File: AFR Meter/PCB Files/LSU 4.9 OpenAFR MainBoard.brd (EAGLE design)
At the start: 62 x 83.5 mm, 82 parts, among them IC2 LMV321M5X, IC3 MCP4725A2T-E_CH, IC4 ATMEGA328PB-AN, IC5 ISO6520DR, IC6 7805DT, IC7 MCP25625-E_SS, Q1 BUK7Y6R0-60EX

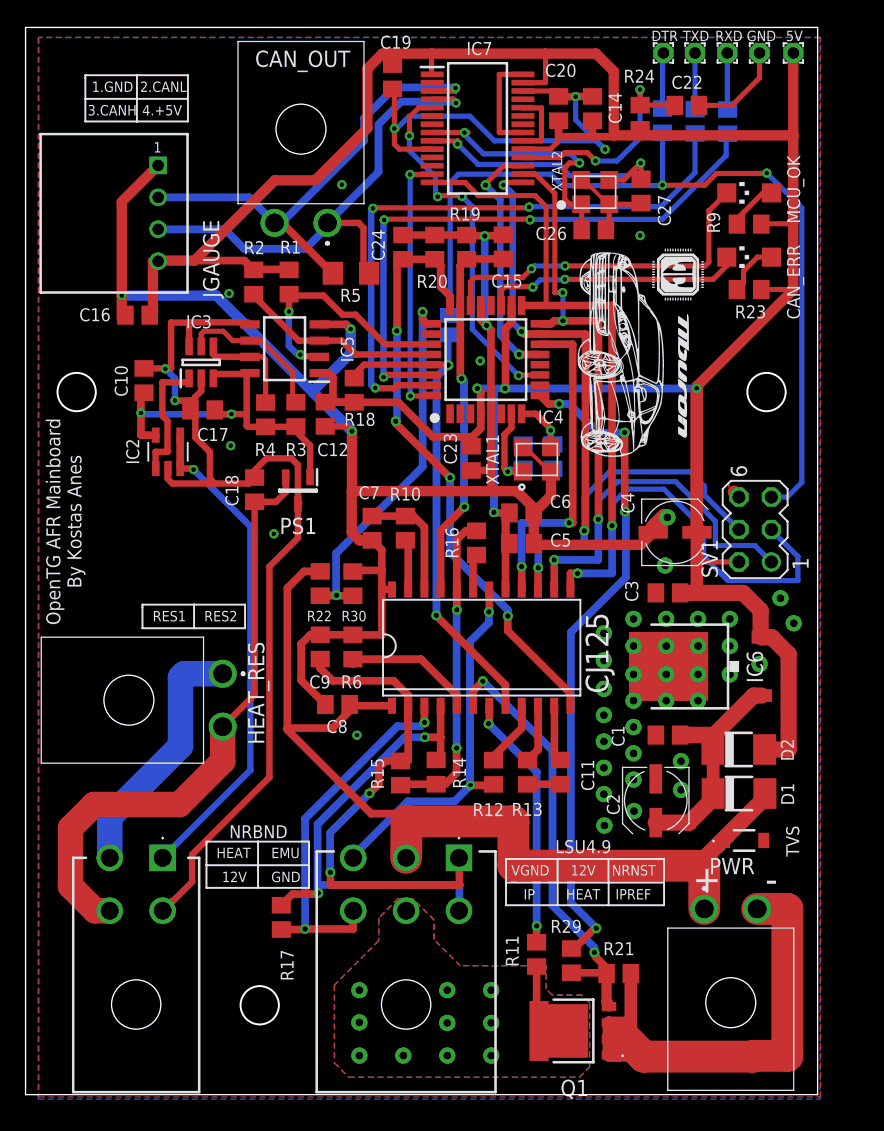
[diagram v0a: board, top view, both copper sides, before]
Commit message: QoL changes for optimizing production
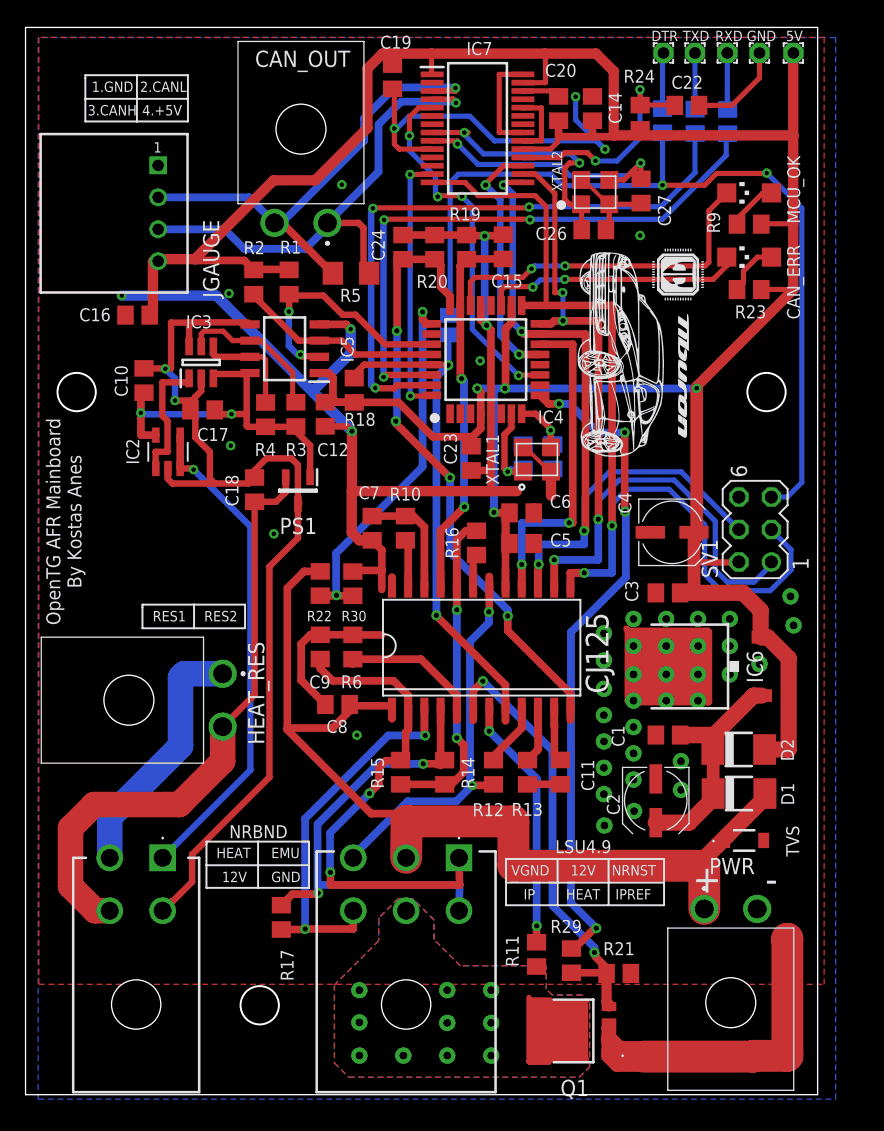
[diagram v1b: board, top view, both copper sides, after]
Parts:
- moved R14 0.67 mm to (32.8, 25.2)
- moved C4 0.23 mm to (50.6, 44.0)
- moved R15 0.06 mm to (29.4, 25.2)
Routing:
- net GND: track 256.8 -> 237.2 mm, vias 49 -> 47
- net LSU_HEAT: track 7.53 -> 17.0 mm
- net SPI_MISO: track 62.2 -> 65.0 mm
- net LSU_IPREF: track 40.7 -> 39.3 mm
- net RESET: track 108.4 -> 109.5 mm
- net LSU_VGND: track 29.4 -> 30.6 mm
- net HEAT_GATE: track 34.6 -> 35.7 mm
- net N$7: track 10.5 -> 11.7 mm
- net UR: track 47.9 -> 49.0 mm
- net +12V: track 80.5 -> 81.5 mm
- net USUP: track 24.9 -> 25.8 mm
- net LSU_IP: track 29.6 -> 30.3 mm

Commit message: Mainboard power supply and QoL updates.
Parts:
- removed C2, C4: 10uF, rcl:UD-5X5,8_NICHICON
- removed IC6: 7805DT, linear:TO252
- added C28: 10uF, rcl:C0805
- added C29, C30: (no value), rcl:153CLV-0605
- added IC1: MC7805CD2TR4G, MC7805CD2TR4G:MC7805CD2TR4G
- moved C3 2.40 mm to (50.9, 41.6)
- moved SV1 2.28 mm to (57.5, 46.5)
- moved C1 1.15 mm to (50.6, 27.0)
- moved C8 0.77 mm to (23.6, 30.5)
- moved C9 0.77 mm to (22.3, 35.0)
- moved R22 0.77 mm to (22.3, 40.0)
- moved R30 0.77 mm to (24.9, 40.0)
- moved R6 0.77 mm to (24.9, 35.0)
- moved U$1 0.72 mm to (35.1, 35.1)
- moved C5 0.67 mm to (39.4, 43.5)
- moved R10 0.58 mm to (29.3, 44.7)
- moved C6 0.55 mm to (39.4, 45.6)
- moved C7 0.43 mm to (26.9, 44.7)
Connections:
- new net N$4: C21.1, RESET.1
- net +5V: now also C29.+, IC1.3; no longer C4.+, IC6.2
- net 5V_ISO: now also C28.1
- net GND: now also C29.-, C30.-, IC1.2; no longer C2.-, C4.-, IC6.3
- net N$6: now also C30.+, IC1.1; no longer C2.+, IC6.1
- net NRBND_GND: now also C28.2
- net RESET: no longer C21.1, RESET.1, SV1.5
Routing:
- net GND: track 237.2 -> 132.8 mm, vias 47 -> 45
- net RESET: track 109.5 -> 41.3 mm, vias 4 -> 2
- net N$4: track 0.00 -> 30.0 mm
- net LSU_HEAT: track 17.0 -> 32.0 mm
- net +5V: track 240.8 -> 252.8 mm, vias 4 -> 6
- net LSU_VNERNST: track 43.8 -> 38.6 mm
- net NRBND_GND: track 80.1 -> 83.7 mm
- net SPI_CLK: track 76.2 -> 72.9 mm
- net SPI_MISO: track 65.0 -> 62.1 mm
- net SPI_MOSI: track 59.8 -> 57.0 mm
- net SPI_CS1: track 25.8 -> 23.6 mm
- net CAN_STBY: track 28.8 -> 30.6 mm, vias 4 -> 2
- net +12V: track 81.5 -> 83.2 mm
- net 5V_ISO: track 31.0 -> 32.7 mm
- net USUP: track 25.8 -> 26.9 mm
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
